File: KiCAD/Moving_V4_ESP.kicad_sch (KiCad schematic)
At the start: 90 parts, among them J1 Vin_1, J10 Conn_01x03_Pin, J11 Conn_01x03_Pin, J12 Conn_01x03_Pin, J13 Conn_01x03_Pin, J2 Vin_2, J3 Power_SW, J4 USB_B_Micro, J5 MOTOR_R, J6 Motor_L, J7 Conn_01x04_Pin, J8 Conn_01x04_Pin, J9 Vin_XT, Q1 U4_ALT2, Q2 U4_ALT2, Q3 U4_ALT2, SW1 SW_Reset, U1 CH340X, U10 TXB0104RUT, U2 UZ1085L-33-TN3-R, U3 ESP32-WROOM-32, U4 ITR8307-S17-TR8, U5 ITR8307-S17-TR8, U6 ITR8307-S17-TR8, U7 CP3119MDTR, U8 CP2119LDTR, U9 SE8650K2B-HF

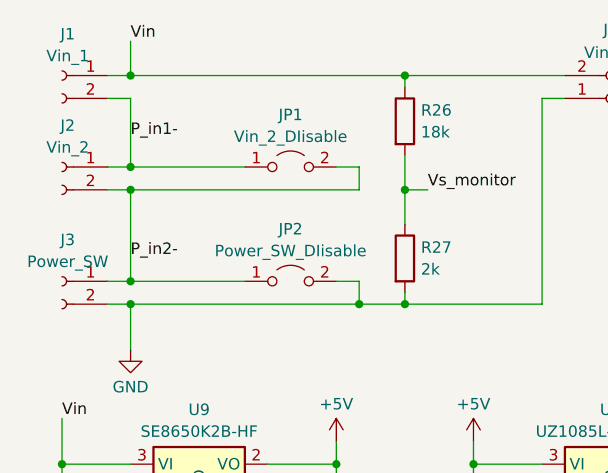
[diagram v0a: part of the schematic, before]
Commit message: 電源コネクタを一つ削除
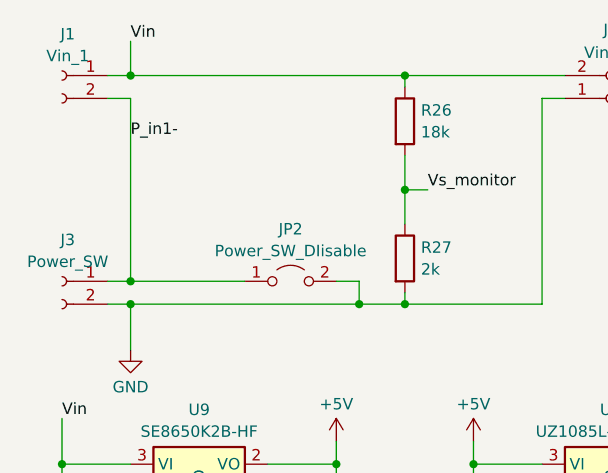
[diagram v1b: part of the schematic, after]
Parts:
- removed J2: Vin_2, Connector_JST:JST_PH_B2B-PH-K_1x02_P2.00mm_Vertical, symbol Connector:Conn_01x02_Socket
- removed JP1: Vin_2_DIisable, Jumper:SolderJumper-2_P1.3mm_Open_RoundedPad1.0x1.5mm, symbol Jumper:Jumper_2_Open
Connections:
- net P_in2- is gone; now on net P_in1-: J3.1 (Pin_1), JP2.1 (A)
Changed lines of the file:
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@@
   (junction (at 63.5 63.5) (diameter 0) (color 0 0 0 0)
   )
-  (junction (at 25.4 33.02) (diameter 0) (color 0 0 0 0)
-  )
-  (junction (at 25.4 30.48) (diameter 0) (color 0 0 0 0)
-  )
   (junction (at 88.9 33.02) (diameter 0) (color 0 0 0 0)
   )
@@
     (stroke (width 0) (type default))
   )
-  (wire (pts (xy 25.4 33.02) (xy 50.8 33.02))
-    (stroke (width 0) (type default))
-  )
   (wire (pts (xy 30.48 106.68) (xy 36.83 106.68))
     (stroke (width 0) (type default))
@@
     (stroke (width 0) (type default))
   )
-  (wire (pts (xy 50.8 30.48) (xy 50.8 33.02))
-    (stroke (width 0) (type default))
-  )
-  (wire (pts (xy 25.4 30.48) (xy 38.1 30.48))
-    (stroke (width 0) (type default))
-  )
   (wire (pts (xy 228.6 73.66) (xy 228.6 80.01))
     (stroke (width 0) (type default))
@@
     (stroke (width 0) (type default))
   )
-  (wire (pts (xy 25.4 22.86) (xy 25.4 30.48))
+  (wire (pts (xy 25.4 22.86) (xy 25.4 43.18))
     (stroke (width 0) (type default))
   )
@@
     (stroke (width 0) (type default))
   )
-  (wire (pts (xy 22.86 33.02) (xy 25.4 33.02))
-    (stroke (width 0) (type default))
-  )
   (wire (pts (xy 40.64 165.1) (xy 40.64 162.56))
     (stroke (width 0) (type default))
@@
     (stroke (width 0) (type default))
   )
-  (wire (pts (xy 48.26 30.48) (xy 50.8 30.48))
-    (stroke (width 0) (type default))
-  )
   (wire (pts (xy 48.26 63.5) (xy 48.26 67.31))
     (stroke (width 0) (type default))
@@
     (stroke (width 0) (type default))
   )
-  (wire (pts (xy 25.4 30.48) (xy 22.86 30.48))
-    (stroke (width 0) (type default))
-  )
   (wire (pts (xy 213.36 134.62) (xy 217.17 134.62))
     (stroke (width 0) (type default))
@@
     (stroke (width 0) (type default))
   )
-  (wire (pts (xy 25.4 33.02) (xy 25.4 43.18))
-    (stroke (width 0) (type default))
-  )
   (wire (pts (xy 63.5 60.96) (xy 63.5 63.5))
     (stroke (width 0) (type default))
@@
     (effects (font (size 1.27 1.27)) (justify left bottom))
   )
-  (label "P_in2-" (at 25.4 40.64 0) (fields_autoplaced)
-    (effects (font (size 1.27 1.27)) (justify left bottom))
-  )
   (label "MTDO" (at 170.18 83.82 0) (fields_autoplaced)
     (effects (font (size 1.27 1.27)) (justify left bottom))
@@
     )
   )
-  (symbol (lib_id "Jumper:Jumper_2_Open") (at 43.18 30.48 0) (unit 1)
-    (in_bom yes) (on_board yes) (dnp no) (fields_autoplaced)
-    (property "Reference" "JP1" (at 43.18 24.6847 0)
-      (effects (font (size 1.27 1.27)))
-    )
-    (property "Value" "Vin_2_DIisable" (at 43.18 27.1089 0)
-      (effects (font (size 1.27 1.27)))
-    )
-    (property "Footprint" "Jumper:SolderJumper-2_P1.3mm_Open_RoundedPad1.0x1.5mm" (at 43.18 30.48 0)
-      (effects (font (size 1.27 1.27)) hide)
-    )
-    (property "Datasheet" "~" (at 43.18 30.48 0)
-      (effects (font (size 1.27 1.27)) hide)
-    )
-    (property "LCSC" "x" (at 43.18 30.48 0)
-      (effects (font (size 1.27 1.27)) hide)
-    )
-    (pin "1")
-    (pin "2")
-    (instances
-      (project "Moving_V4_ESP"
-        (path "/515135d2-db88-48ff-b508-cbebeed2b019"
-          (reference "JP1") (unit 1)
-        )
-      )
-    )
-  )
   (symbol (lib_id "Device:LED") (at 218.44 149.86 90) (unit 1)
     (in_bom yes) (on_board yes) (dnp no) (fields_autoplaced)
@@
         )
       )
-    )
-  )
-  (symbol (lib_id "Connector:Conn_01x02_Socket") (at 17.78 30.48 0) (mirror y) (unit 1)
-    (in_bom yes) (on_board yes) (dnp no) (fields_autoplaced)
-    (property "Reference" "J2" (at 18.415 25.8785 0)
-      (effects (font (size 1.27 1.27)))
-    )
-    (property "Value" "Vin_2" (at 18.415 28.3027 0)
-      (effects (font (size 1.27 1.27)))
-    )
-    (property "Footprint" "Connector_JST:JST_PH_B2B-PH-K_1x02_P2.00mm_Vertical" (at 17.78 30.48 0)
-      (effects (font (size 1.27 1.27)) hide)
-    )
-    (property "Datasheet" "~" (at 17.78 30.48 0)
-      (effects (font (size 1.27 1.27)) hide)
-    )
-    (property "LCSC" "C160352" (at 17.78 30.48 0)
-      (effects (font (size 1.27 1.27)) hide)
-    )
-    (pin "1")
-    (pin "2")
-    (instances
-      (project "Moving_V4_ESP"
-        (path "/515135d2-db88-48ff-b508-cbebeed2b019"
-          (reference "J2") (unit 1)
-        )
-      )

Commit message: アノテーションを再実行
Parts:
- J10: renamed from J11; value Conn_01x03_Pin -> IO27_GPIO1
- J11: renamed from J12; value Conn_01x03_Pin -> IO32_GPIO2
- J12: renamed from J13; value Conn_01x03_Pin -> IO5_GPIO3(PU)
- J5: renamed from J7; value Conn_01x04_Pin -> Encorder_L
- J6: renamed from J8; value Conn_01x04_Pin -> Encorder_R
- J7: renamed from J6; value Motor_L -> MOTOR_L
- J9: renamed from J10; value Conn_01x03_Pin -> IO4_GPIO0
- JP4: renamed from JP11; value L1_PU -> R1_PU
- JP5: renamed from JP12; value L2_PU -> R2_PU
- U6: renamed from U8; value CP2119LDTR -> CP3119MDTR
- renumbered C11 to C1, C7 to C10, C6 to C11, C8 to C12, C12 to C2, C2 to C3, C3 to C4, C1 to C5, C4 to C6, C10 to C7, C9 to C8, C5 to C9, D5 to D1, D1 to D2, D2 to D3, D3 to D4, D4 to D5, J3 to J2, J9 to J3, J5 to J8, JP2 to JP1, JP3 to JP10, JP4 to JP11, JP5 to JP12, JP6 to JP13, JP7 to JP14, JP8 to JP15, JP9 to JP2, JP10 to JP3, JP13 to JP6, JP14 to JP7, JP15 to JP8, JP16 to JP9, R26 to R1, R19 to R10, R17 to R11, R20 to R12, R18 to R13, R3 to R14, R4 to R15, R5 to R16, R21 to R17, R22 to R18, R23 to R19, R27 to R2, R24 to R20, R6 to R21, R9 to R22, R7 to R23, R10 to R24, R8 to R25, R11 to R26, R12 to R3, R13 to R4, R1 to R5, R16 to R6, R14 to R7, R15 to R8, R2 to R9, U9 to U1, U6 to U10, U1 to U2, U2 to U3, U10 to U4, U7 to U5, U3 to U7, U4 to U8, U5 to U9

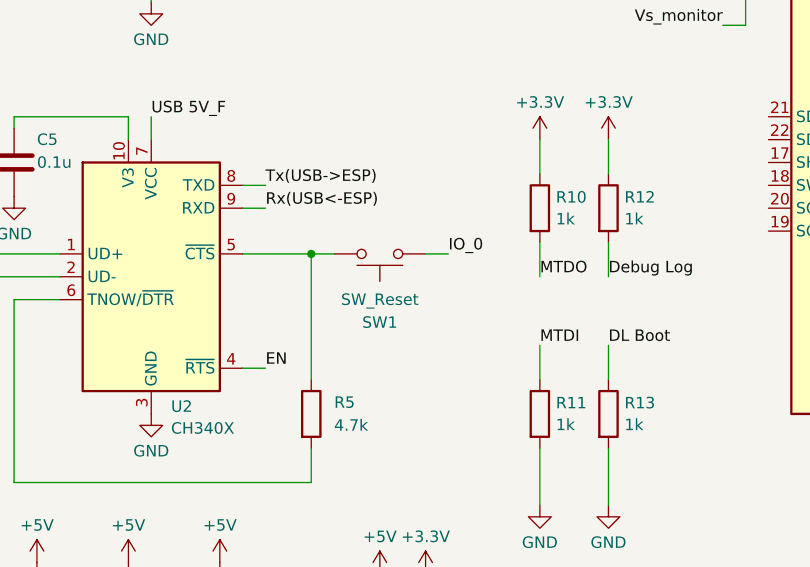
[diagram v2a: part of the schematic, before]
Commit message: モード切替スイッチを削除
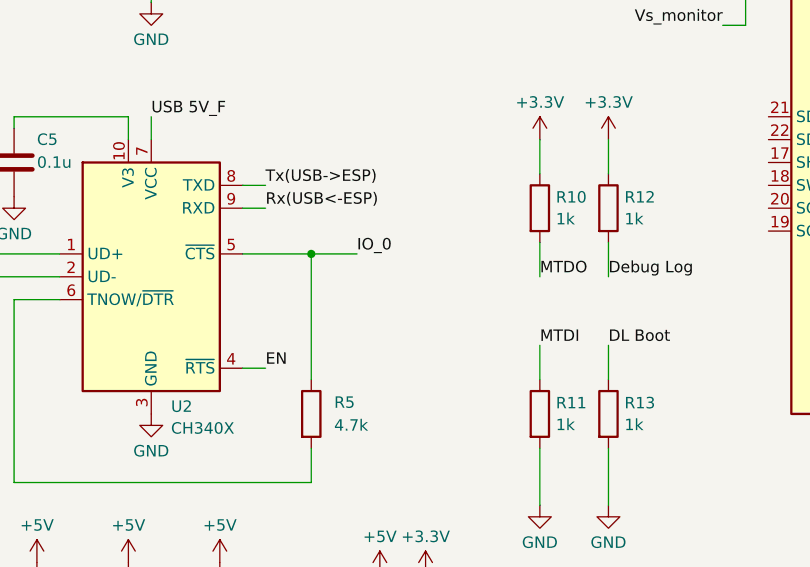
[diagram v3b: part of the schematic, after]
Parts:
- removed SW1: SW_Reset, Button_Switch_SMD:SW_Push_1P1T_XKB_TS-1187A, symbol Switch:SW_Omron_B3FS
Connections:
- net IO_0: now also R5.1, U2.5 (~{CTS})
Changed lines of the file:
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@@
     (stroke (width 0) (type default))
   )
-  (wire (pts (xy 93.98 106.68) (xy 96.52 106.68))
-    (stroke (width 0) (type default))
-  )
   (wire (pts (xy 50.8 148.59) (xy 50.8 149.86))
     (stroke (width 0) (type default))
@@
     (stroke (width 0) (type default))
   )
-  (wire (pts (xy 83.82 106.68) (xy 81.28 106.68))
+  (wire (pts (xy 81.28 106.68) (xy 86.36 106.68))
     (stroke (width 0) (type default))
   )
@@
     (effects (font (size 1.27 1.27)) (justify left bottom))
   )
-  (label "IO_0" (at 96.52 106.68 0) (fields_autoplaced)
+  (label "IO_0" (at 86.36 106.68 0) (fields_autoplaced)
     (effects (font (size 1.27 1.27)) (justify left bottom))
   )
@@
         )
       )
-    )
-  )
-  (symbol (lib_id "Switch:SW_Omron_B3FS") (at 88.9 106.68 0) (mirror x) (unit 1)
-    (in_bom yes) (on_board yes) (dnp no)
-    (property "Reference" "SW1" (at 88.9 114.3 0)
-      (effects (font (size 1.27 1.27)))
-    )
-    (property "Value" "SW_Reset" (at 88.9 111.76 0)
-      (effects (font (size 1.27 1.27)))
-    )
-    (property "Footprint" "Button_Switch_SMD:SW_Push_1P1T_XKB_TS-1187A" (at 88.9 111.76 0)
-      (effects (font (size 1.27 1.27)) hide)
-    )
-    (property "Datasheet" "https://omronfs.omron.com/en_US/ecb/products/pdf/en-b3fs.pdf" (at 88.9 111.76 0)
-      (effects (font (size 1.27 1.27)) hide)
-    )
-    (property "LCSC" "C318884" (at 88.9 106.68 0)
-      (effects (font (size 1.27 1.27)) hide)
-    )
-    (pin "1")
-    (pin "2")
-    (instances
-      (project "Moving_V4_ESP"
-        (path "/515135d2-db88-48ff-b508-cbebeed2b019"
-          (reference "SW1") (unit 1)
-        )
-      )

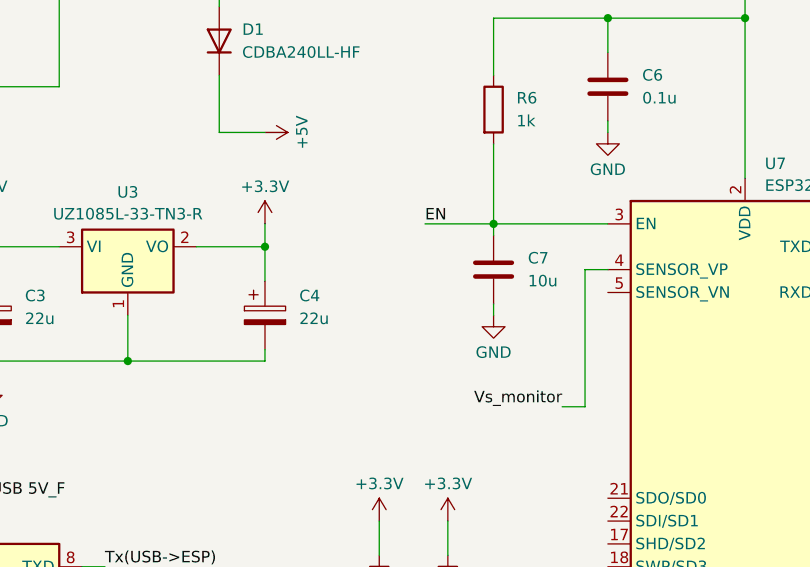
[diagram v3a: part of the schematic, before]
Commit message: リセット用のジャンパー追加
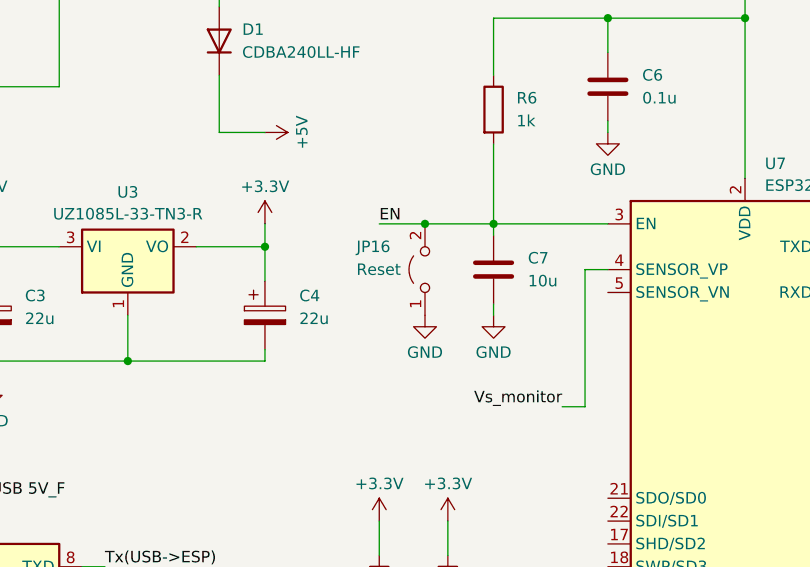
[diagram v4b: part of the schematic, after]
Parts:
- added JP16: Reset, Jumper:SolderJumper-2_P1.3mm_Open_RoundedPad1.0x1.5mm, symbol Jumper:Jumper_2_Open
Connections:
- net EN: now also JP16.2 (B)
- net GND: now also JP16.1 (A)
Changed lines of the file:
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@@
   (junction (at 121.285 153.67) (diameter 0) (color 0 0 0 0)
   )
+  (junction (at 111.76 60.96) (diameter 0) (color 0 0 0 0)
+  )
   (junction (at 17.78 63.5) (diameter 0) (color 0 0 0 0)
   )
@@
     (stroke (width 0) (type default))
   )
-  (wire (pts (xy 111.76 60.96) (xy 119.38 60.96))
+  (wire (pts (xy 106.68 60.96) (xy 111.76 60.96))
     (stroke (width 0) (type default))
   )
@@
     (stroke (width 0) (type default))
   )
+  (wire (pts (xy 111.76 60.96) (xy 119.38 60.96))
+    (stroke (width 0) (type default))
+  )
   (wire (pts (xy 228.6 73.66) (xy 228.6 80.01))
     (stroke (width 0) (type default))
@@
     (effects (font (size 1.27 1.27)) (justify left bottom))
   )
-  (label "EN" (at 111.76 60.96 0) (fields_autoplaced)
+  (label "EN" (at 106.68 60.96 0) (fields_autoplaced)
     (effects (font (size 1.27 1.27)) (justify left bottom))
   )
@@
     )
   )
+  (symbol (lib_id "Jumper:Jumper_2_Open") (at 111.76 66.04 90) (unit 1)
+    (in_bom yes) (on_board yes) (dnp no)
+    (property "Reference" "JP16" (at 104.14 63.5 90)
+      (effects (font (size 1.27 1.27)) (justify right))
+    )
+    (property "Value" "Reset" (at 104.14 66.04 90)
+      (effects (font (size 1.27 1.27)) (justify right))
+    )
+    (property "Footprint" "Jumper:SolderJumper-2_P1.3mm_Open_RoundedPad1.0x1.5mm" (at 111.76 66.04 0)
+      (effects (font (size 1.27 1.27)) hide)
+    )
+    (property "Datasheet" "~" (at 111.76 66.04 0)
+      (effects (font (size 1.27 1.27)) hide)
+    )
+    (property "LCSC" "x" (at 111.76 66.04 0)
+      (effects (font (size 1.27 1.27)) hide)
+    )
+    (pin "1")
+    (pin "2")
+    (instances
+      (project "Moving_V4_ESP"
+        (path "/515135d2-db88-48ff-b508-cbebeed2b019"
+          (reference "JP16") (unit 1)
+        )
+      )
+    )
+  )
   (symbol (lib_id "Connector:Conn_01x03_Pin") (at 220.98 40.64 0) (unit 1)
     (in_bom yes) (on_board yes) (dnp no) (fields_autoplaced)
@@
         )
       )
+    )
+  )
+  (symbol (lib_id "power:GND") (at 111.76 71.12 0) (unit 1)
+    (in_bom yes) (on_board yes) (dnp no) (fields_autoplaced)
+    (property "Reference" "#PWR048" (at 111.76 77.47 0)
+      (effects (font (size 1.27 1.27)) hide)
+    )
+    (property "Value" "GND" (at 111.76 75.2531 0)
+      (effects (font (size 1.27 1.27)))
+    )
+    (property "Footprint" "" (at 111.76 71.12 0)
+      (effects (font (size 1.27 1.27)) hide)
+    )
+    (property "Datasheet" "" (at 111.76 71.12 0)
+      (effects (font (size 1.27 1.27)) hide)
+    )
+    (pin "1")
+    (instances
+      (project "Moving_V4_ESP"
+        (path "/515135d2-db88-48ff-b508-cbebeed2b019"
+          (reference "#PWR048") (unit 1)
+        )
+      )

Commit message: 電解コンデンサをDIP部品に変更
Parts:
- C3, C4: footprint Capacitor_SMD:CP_Elec_6.3x5.4 -> Capacitor_THT:CP_Radial_D5.0mm_P2.00mm; LCSC C131161 -> (none)
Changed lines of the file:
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@@
       (effects (font (size 1.27 1.27)) (justify left))
     )
-    (property "Footprint" "Capacitor_SMD:CP_Elec_6.3x5.4" (at 94.9452 74.93 0)
+    (property "Footprint" "Capacitor_THT:CP_Radial_D5.0mm_P2.00mm" (at 94.9452 74.93 0)
       (effects (font (size 1.27 1.27)) hide)
     )
@@
       (effects (font (size 1.27 1.27)) hide)
     )
-    (property "LCSC" "C131161" (at 93.98 71.12 0)
+    (property "LCSC" "" (at 93.98 71.12 0)
       (effects (font (size 1.27 1.27)) hide)
     )
@@
       (effects (font (size 1.27 1.27)) (justify left))
     )
-    (property "Footprint" "Capacitor_SMD:CP_Elec_6.3x5.4" (at 64.4652 74.93 0)
+    (property "Footprint" "Capacitor_THT:CP_Radial_D5.0mm_P2.00mm" (at 64.4652 74.93 0)
       (effects (font (size 1.27 1.27)) hide)
     )
@@
       (effects (font (size 1.27 1.27)) hide)
     )
-    (property "LCSC" "C131161" (at 63.5 71.12 0)
+    (property "LCSC" "" (at 63.5 71.12 0)
       (effects (font (size 1.27 1.27)) hide)
     )

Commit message: 部品表に秋月の商品コードを追加
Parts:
- C11, C9: 秋月 (none) -> 102719
- C3, C4: LCSC (none) -> x; 秋月 (none) -> 117899
- D2, D5: 秋月 (none) -> 111637
- D3: 秋月 (none) -> 111577
- D4: 秋月 (none) -> 112610
- D6, D7, D8: footprint LED_THT:LED_D5.0mm -> LED_THT:LED_D3.0mm; LCSC (none) -> x; 秋月 (none) -> 104313
- J1, J2: LCSC C160352 -> x; 秋月 (none) -> 112802
- J10, J11, J12, J9: LCSC (none) -> x; 秋月 (none) -> 100167
- J3: LCSC C160352 -> x; 秋月 (none) -> 117952
- J5, J6: LCSC (none) -> x; 秋月 (none) -> 114157
- J7, J8: LCSC C8465 -> x; 秋月 (none) -> 101306
- JP1, JP16: 秋月 (none) -> x
- JP10, JP11, JP12, JP13, JP14, JP15, JP2, JP3, JP4, JP5, JP6, JP7, JP8, JP9: LCSC (none) -> x; 秋月 (none) -> x
- Q1, Q2, Q3: footprint LED_THT:LED_D5.0mm -> LED_THT:LED_D3.0mm; LCSC (none) -> x; 秋月 (none) -> 104213
- U4: LCSC (none) -> C105266
- U7: LCSC - -> x; 秋月 (none) -> 115675
